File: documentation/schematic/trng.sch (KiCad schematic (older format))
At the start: 11 parts

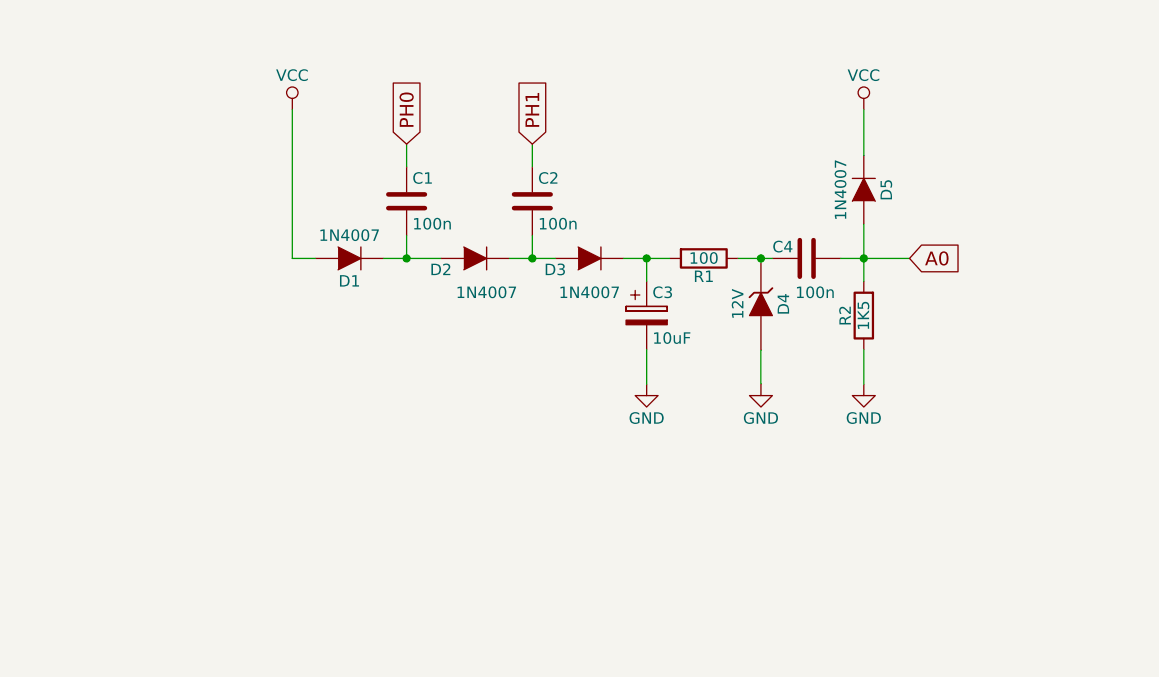
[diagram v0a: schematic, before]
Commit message: Update schematics, better generation code
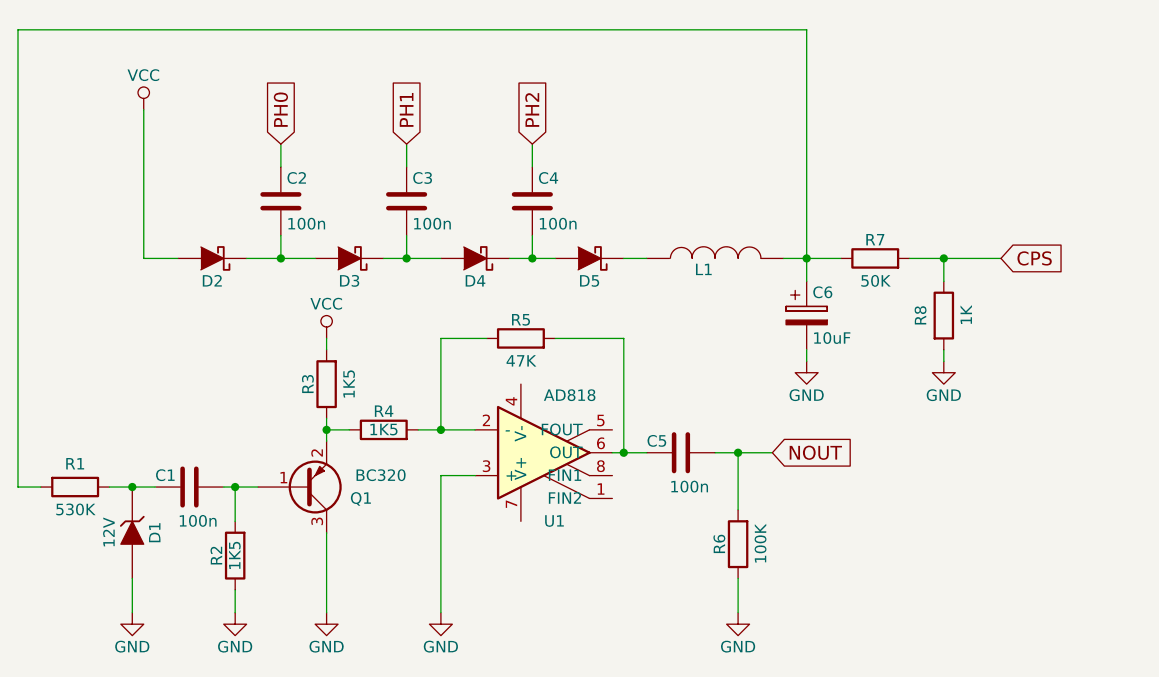
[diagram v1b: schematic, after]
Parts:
- removed D1, D2, D3, D5: 1N4007, symbol D
- added C2, C5: 100n, symbol C
- added D2, D3, D4, D5: D_Schottky, symbol D_Schottky
- added L1: INDUCTOR, symbol INDUCTOR
- added Q1: BC320, symbol Q_PNP_BEC
- added R3, R4: 1K5, symbol R
- added R5: 47K, symbol R
- added R6: 100K, symbol R
- added R7: 50K, symbol R
- added R8: 1K, symbol R
- added U1: AD818, symbol LM318N
- R1: value 100 -> 530K
- renumbered C4 to C1, C1 to C3, C2 to C4, C3 to C6, D4 to D1
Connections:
- net GND: now also Q1.3 (C), R6.1, R8.2, U1.3 (+)
- net PH0: now also C2.1; no longer C3.1
- net PH1: now also C3.1; no longer C4.1
- net VCC: now also D2.2 (A), R3.2
- net at C6.1, R1.2: now also L1.2, R7.1
- net at C4.2: now also D4.1 (K), D5.2 (A)
- net at C3.2: now also D3.1 (K), D4.2 (A)
- net A0: no longer names the net of C1.1, R2.2
- net A0: now also Q1.1 (B)
- new net: C2.2, D2.1 (K), D3.2 (A)
- new net: D5.1 (K), L1.1
- new net: Q1.2 (E), R3.1, R4.1
- new net: R4.2, R5.1, U1.2 (-)
- new net: C5.2, R5.2, U1.6 (OUT)
- new net CPS: R7.2, R8.1
- new net NOUT: C5.1, R6.2
- new net PH2: C4.1
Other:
- moved on the sheet: C1, C6, D1, R1

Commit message: Update schematic
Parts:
- removed C5: 100n, symbol C
- removed Q1: BC320, symbol Q_PNP_BEC
- removed R3, R4: 1K5, symbol R
- removed R5: 47K, symbol R
- removed R6: 100K, symbol R
- removed U1: AD818, symbol LM318N
- renumbered C6 to C5, R7 to R3, R8 to R4
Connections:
- net NOUT: now also C1.1, R2.2
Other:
- moved on the sheet: C1, C5, D1, L1, R1, R2, R3, R4
